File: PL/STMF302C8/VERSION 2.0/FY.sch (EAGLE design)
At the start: 64 parts, among them J1 CON-SD-CARD_MICROSD-2908-05, J4 FEMALE 2x3, U1 AS72652-BLGT, U2 AS72653-BLGT, U4 AS72651-BLGT, U5 AMS1117-3.3, U6 4MB Flash, U7 MS561101BA03-50, X1 JST-XH-04-PIN-LONG-PAD, Y2 ABM2B-8.000MHZ-10-1-U-T

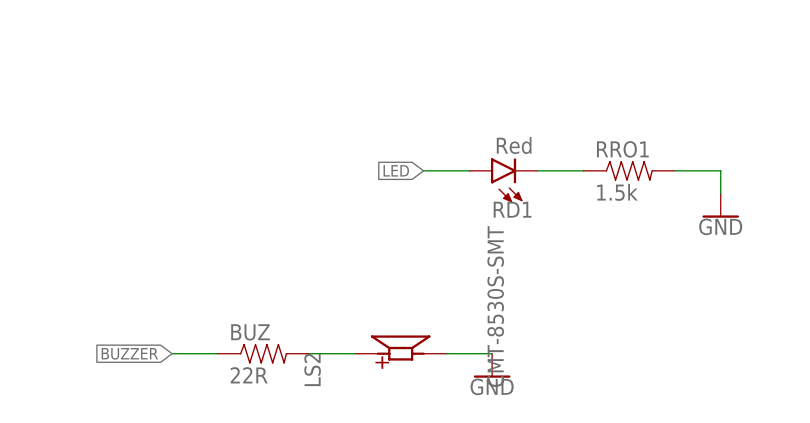
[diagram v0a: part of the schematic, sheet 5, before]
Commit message: distance holl was putted
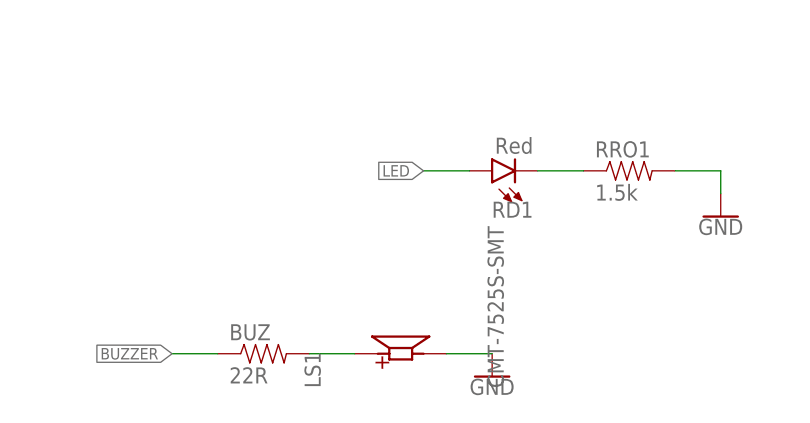
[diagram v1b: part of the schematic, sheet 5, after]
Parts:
- removed LS2: CMT-8530S-SMT, SMT-BUZZER:CMT-8530S-SMT
- added LS1: CMT-7525S-SMT, CMT-7525S-SMT:CMT-7525S-SMT
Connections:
- net GND: now also LS1.N; no longer LS2.N
- net N$9: now also LS1.P; no longer LS2.P
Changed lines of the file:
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@@
 <part name="J5" library="SparkFun-Connectors" library_urn="urn:adsk.eagle:library:513" deviceset="USB_AB" device="_SMT" package3d_urn="urn:adsk.eagle:package:38266/1"/>
 <part name="SUPPLY34" library="SparkFun-PowerSymbols" library_urn="urn:adsk.eagle:library:530" deviceset="VIN" device="" value="VINR"/>
-<part name="LS2" library="SMT-BUZZER" deviceset="CMT-8530S-SMT" device=""/>
+<part name="LS1" library="CMT-7525S-SMT" deviceset="CMT-7525S-SMT" device=""/>
 </parts>
 <sheets>
@@
 <attribute name="VALUE" x="78.74" y="75.946" size="1.778" layer="96" rot="R180" align="bottom-center"/>
 </instance>
-<instance part="LS2" gate="G$1" x="83.82" y="25.4" smashed="yes" rot="R90">
-<attribute name="NAME" x="74.922090625" y="21.586609375" size="1.77958125" layer="95" rot="R90"/>
-<attribute name="VALUE" x="95.2648" y="21.585059375" size="1.780309375" layer="96" rot="R90"/>
+<instance part="LS1" gate="G$1" x="83.82" y="25.4" smashed="yes" rot="R90">
+<attribute name="NAME" x="74.928159375" y="21.589209375" size="1.77836875" layer="95" rot="R90"/>
+<attribute name="VALUE" x="95.2674" y="21.58418125" size="1.780709375" layer="96" rot="R90"/>
 </instance>
 </instances>
@@
 </segment>
 <segment>
-<pinref part="LS2" gate="G$1" pin="N"/>
 <pinref part="GND23" gate="1" pin="GND"/>
 <wire x1="88.9" y1="25.4" x2="93.98" y2="25.4" width="0.1524" layer="91"/>
+<pinref part="LS1" gate="G$1" pin="N"/>
 </segment>
 </net>
@@
 <segment>
 <pinref part="BUZ" gate="G$1" pin="2"/>
-<pinref part="LS2" gate="G$1" pin="P"/>
 <wire x1="73.66" y1="25.4" x2="78.74" y2="25.4" width="0.1524" layer="91"/>
-</segment>
-</net>
+<pinref part="LS1" gate="G$1" pin="P"/>
+</segment>
+</net>

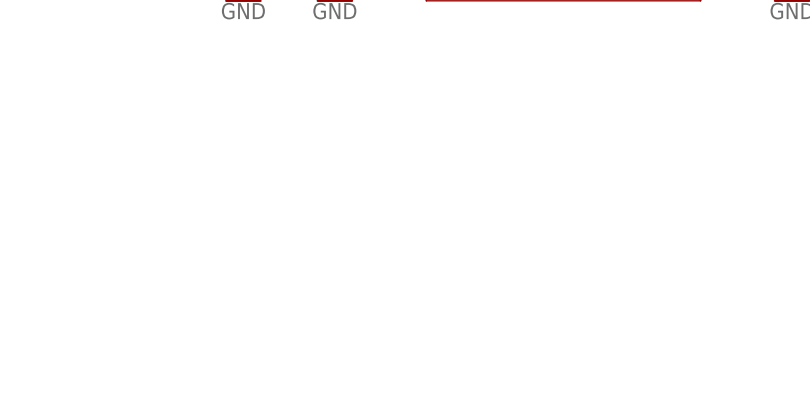
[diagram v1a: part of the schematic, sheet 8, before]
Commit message: Magnetometer was added by brain.dll
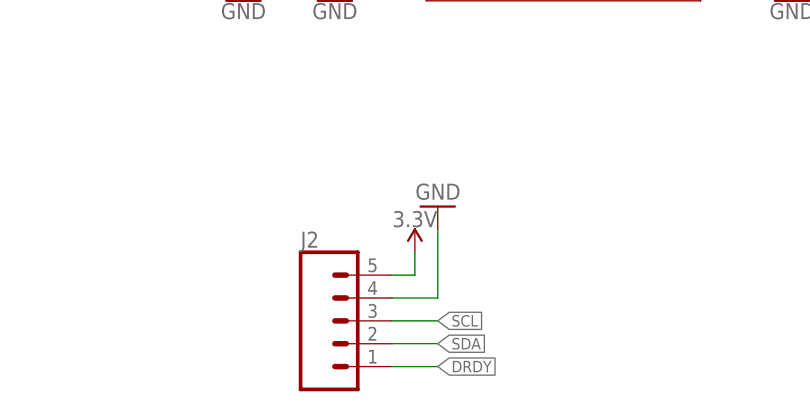
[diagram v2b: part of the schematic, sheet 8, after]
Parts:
- added J2: (no value), SparkFun-Connectors:CONN_05LOCK_LONGPADS
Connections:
- new net DRDY: J2.1, U8A.PC13
- net 3.3V: now also J2.5
- net GND: now also J2.4
- net SCL: now also J2.3
- net SDA: now also J2.2
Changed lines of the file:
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@@
 <part name="SUPPLY34" library="SparkFun-PowerSymbols" library_urn="urn:adsk.eagle:library:530" deviceset="VIN" device="" value="VINR"/>
 <part name="LS1" library="CMT-7525S-SMT" deviceset="CMT-7525S-SMT" device=""/>
+<part name="J2" library="SparkFun-Connectors" library_urn="urn:adsk.eagle:library:513" deviceset="CONN_05" device="LOCK_LONGPADS" package3d_urn="urn:adsk.eagle:package:38107/1"/>
+<part name="GND31" library="supply1" library_urn="urn:adsk.eagle:library:371" deviceset="GND" device=""/>
+<part name="SUPPLY35" library="SparkFun-PowerSymbols" library_urn="urn:adsk.eagle:library:530" deviceset="3.3V" device=""/>
 </parts>
 <sheets>
@@
 <wire x1="27.94" y1="127" x2="22.86" y2="127" width="0.1524" layer="91"/>
 <label x="22.86" y="127" size="1.27" layer="95" rot="R180" xref="yes"/>
+</segment>
+</net>
+<net name="DRDY" class="0">
+<segment>
+<pinref part="U8" gate="A" pin="PC13"/>
+<wire x1="88.9" y1="116.84" x2="93.98" y2="116.84" width="0.1524" layer="91"/>
+<label x="93.98" y="116.84" size="1.27" layer="95" xref="yes"/>
 </segment>
 </net>
@@
 <instance part="SUPPLY9" gate="G$1" x="48.26" y="106.68" smashed="yes">
 <attribute name="VALUE" x="48.26" y="109.474" size="1.778" layer="96" align="bottom-center"/>
+</instance>
+<instance part="J2" gate="G$1" x="96.52" y="48.26" smashed="yes">
+<attribute name="VALUE" x="93.98" y="38.354" size="1.778" layer="96" font="vector"/>
+<attribute name="NAME" x="93.98" y="56.388" size="1.778" layer="95" font="vector"/>
+</instance>
+<instance part="GND31" gate="1" x="109.22" y="60.96" smashed="yes" rot="R180">
+<attribute name="VALUE" x="111.76" y="63.5" size="1.778" layer="96" rot="R180"/>
+</instance>
+<instance part="SUPPLY35" gate="G$1" x="106.68" y="55.88" smashed="yes">
+<attribute name="VALUE" x="106.68" y="58.674" size="1.778" layer="96" align="bottom-center"/>
 </instance>
 </instances>
@@
 <junction x="203.2" y="88.9"/>
 </segment>
+<segment>
+<pinref part="J2" gate="G$1" pin="4"/>
+<wire x1="104.14" y1="50.8" x2="109.22" y2="50.8" width="0.1524" layer="91"/>
+<wire x1="109.22" y1="50.8" x2="109.22" y2="58.42" width="0.1524" layer="91"/>
+<pinref part="GND31" gate="1" pin="GND"/>
+</segment>
 </net>
 <net name="3.3V" class="1">
@@
 <junction x="48.26" y="104.14"/>
 </segment>
+<segment>
+<pinref part="J2" gate="G$1" pin="5"/>
+<wire x1="104.14" y1="53.34" x2="106.68" y2="53.34" width="0.1524" layer="91"/>
+<wire x1="106.68" y1="53.34" x2="106.68" y2="55.88" width="0.1524" layer="91"/>
+<pinref part="SUPPLY35" gate="G$1" pin="3.3V"/>
+</segment>
 </net>
 <net name="SCL" class="0">
@@
 <label x="43.18" y="86.36" size="1.27" layer="95" rot="R270" xref="yes"/>
 </segment>
+<segment>
+<pinref part="J2" gate="G$1" pin="3"/>
+<wire x1="104.14" y1="48.26" x2="109.22" y2="48.26" width="0.1524" layer="91"/>
+<label x="109.22" y="48.26" size="1.27" layer="95" xref="yes"/>
+</segment>
 </net>
 <net name="SDA" class="0">
@@
 <label x="53.34" y="86.36" size="1.27" layer="95" rot="R270" xref="yes"/>
 </segment>
+<segment>
+<pinref part="J2" gate="G$1" pin="2"/>
+<wire x1="104.14" y1="45.72" x2="109.22" y2="45.72" width="0.1524" layer="91"/>
+<label x="109.22" y="45.72" size="1.27" layer="95" xref="yes"/>
+</segment>
 </net>
 <net name="INT1" class="0">
@@
 </segment>
 </net>
+<net name="DRDY" class="0">
+<segment>
+<pinref part="J2" gate="G$1" pin="1"/>
+<wire x1="104.14" y1="43.18" x2="109.22" y2="43.18" width="0.1524" layer="91"/>
+<label x="109.22" y="43.18" size="1.27" layer="95" xref="yes"/>
+</segment>
+</net>

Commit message: holes were moved and VDDA cap value was changed
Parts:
- added C11, C12: 100nF, SparkFun-Capacitors:1.0UF-0603-16V-10%
- added HOLDR, WPR: 10k, SparkFun-Resistors:2.0KOHM1/10W5%(0603)
- added IC1: EN25F40-100GCP-TR, adafruit:WS2811-SOP8
- added U3: BMP280, BMP280:BMP280
- VDDA2: value 100nF -> 10nF
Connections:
- new net CSF: IC1.R, U8A.PB12
- new net HOLD: HOLDR.1, IC1.SET, U8A.PA10
- new net WP: IC1.B, U8A.PA9, WPR.2
- net 3.3V: now also C11.2, C12.2, HOLDR.2, IC1.VDD, U3.CSB, U3.VDD, U3.VDDIO
- net GND: now also C11.1, C12.1, IC1.GND, U3.GND, U3.SDO, WPR.1
- net MISO: now also IC1.G
- net MOSI: now also IC1.DO
- net SCK: now also IC1.DIN
- net SCL: now also U3.SCK
- net SDA: now also U3.SDI
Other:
- note added: "BAROMETRE"

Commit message: 05.07.2021
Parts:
- removed LS1: CMT-7525S-SMT, CMT-7525S-SMT:CMT-7525S-SMT
- added LS2: BUZZER-PTH, SparkFun-Electromechanical:BUZZER-PTH
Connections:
- net GND: now also LS2.2; no longer LS1.N
- net N$9: now also LS2.1; no longer LS1.P
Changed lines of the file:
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@@
 <setting verticaltext="up"/>
 </settings>
-<grid distance="100" unitdist="mil" unit="mil" style="dots" multiple="1" display="yes" altdistance="0.01" altunitdist="inch" altunit="mil"/>
+<grid distance="50" unitdist="mil" unit="mil" style="dots" multiple="1" display="yes" altdistance="0.01" altunitdist="inch" altunit="mil"/>
 <layers>
 <layer number="1" name="Top" color="4" fill="1" visible="no" active="no"/>
@@
 <part name="J5" library="SparkFun-Connectors" library_urn="urn:adsk.eagle:library:513" deviceset="USB_AB" device="_SMT" package3d_urn="urn:adsk.eagle:package:38266/1"/>
 <part name="SUPPLY34" library="SparkFun-PowerSymbols" library_urn="urn:adsk.eagle:library:530" deviceset="VIN" device="" value="VINR"/>
-<part name="LS1" library="CMT-7525S-SMT" deviceset="CMT-7525S-SMT" device=""/>
 <part name="J2" library="SparkFun-Connectors" library_urn="urn:adsk.eagle:library:513" deviceset="CONN_05" device="LOCK_LONGPADS" package3d_urn="urn:adsk.eagle:package:38107/1"/>
 <part name="GND31" library="supply1" library_urn="urn:adsk.eagle:library:371" deviceset="GND" device=""/>
@@
 <part name="C11" library="SparkFun-Capacitors" library_urn="urn:adsk.eagle:library:510" deviceset="1.0UF" device="-0603-16V-10%" package3d_urn="urn:adsk.eagle:package:37414/1" value="100nF"/>
 <part name="C12" library="SparkFun-Capacitors" library_urn="urn:adsk.eagle:library:510" deviceset="1.0UF" device="-0603-16V-10%" package3d_urn="urn:adsk.eagle:package:37414/1" value="100nF"/>
+<part name="LS2" library="SparkFun-Electromechanical" library_urn="urn:adsk.eagle:library:516" deviceset="BUZZER" device="-PTH" package3d_urn="urn:adsk.eagle:package:38558/1"/>
 </parts>
 <sheets>
@@
 <attribute name="VALUE" x="78.74" y="75.946" size="1.778" layer="96" rot="R180" align="bottom-center"/>
 </instance>
-<instance part="LS1" gate="G$1" x="83.82" y="25.4" smashed="yes" rot="R90">
-<attribute name="NAME" x="74.928159375" y="21.589209375" size="1.77836875" layer="95" rot="R90"/>
-<attribute name="VALUE" x="95.2674" y="21.58418125" size="1.780709375" layer="96" rot="R90"/>
+<instance part="LS2" gate="G$1" x="82.55" y="27.94" smashed="yes">
+<attribute name="NAME" x="80.01" y="32.766" size="1.778" layer="95" font="vector"/>
 </instance>
 </instances>
@@
 </segment>
 <segment>
+<pinref part="LS2" gate="G$1" pin="2"/>
 <pinref part="GND23" gate="1" pin="GND"/>
-<wire x1="88.9" y1="25.4" x2="93.98" y2="25.4" width="0.1524" layer="91"/>
-<pinref part="LS1" gate="G$1" pin="N"/>
+<wire x1="85.09" y1="25.4" x2="93.98" y2="25.4" width="0.1524" layer="91"/>
 </segment>
 </net>
@@
 </segment>
 </net>
-<net name="N$9" class="0">
-<segment>
-<pinref part="BUZ" gate="G$1" pin="2"/>
-<wire x1="73.66" y1="25.4" x2="78.74" y2="25.4" width="0.1524" layer="91"/>
-<pinref part="LS1" gate="G$1" pin="P"/>
-</segment>
-</net>
 <net name="INT1" class="0">
 <segment>
@@
 </segment>
 </net>
+<net name="N$9" class="0">
+<segment>
+<pinref part="BUZ" gate="G$1" pin="2"/>
+<pinref part="LS2" gate="G$1" pin="1"/>
+<wire x1="73.66" y1="25.4" x2="82.55" y2="25.4" width="0.1524" layer="91"/>
+</segment>
+</net>
